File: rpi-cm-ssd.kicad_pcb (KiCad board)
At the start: 4 copper layers, 87.3 x 55.1 mm, 121 parts, among them J1 USB_C_Receptacle, J2 Bus_M.2_Socket_M, J3 PD controller EEPROM programm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, J4 ARJM11B1-502-AB-EW2, J5 690-008-221-904, U1 TVS2200DRV, U10 TPS65283-1RGER, U11 TCN75AVUA, U12 TCN75AVUA, U13 MGM210PB32JIA2, U2 TPD4EUSB30, U3 TPD4EUSB30, U4 74LVC1G07SE-7, U5 CAT24C256, U6 TPS25750DRJKT, U7 PAC1951-1, U8 USB2512, U9 SC18IS604PWJ, Y1 24MHz

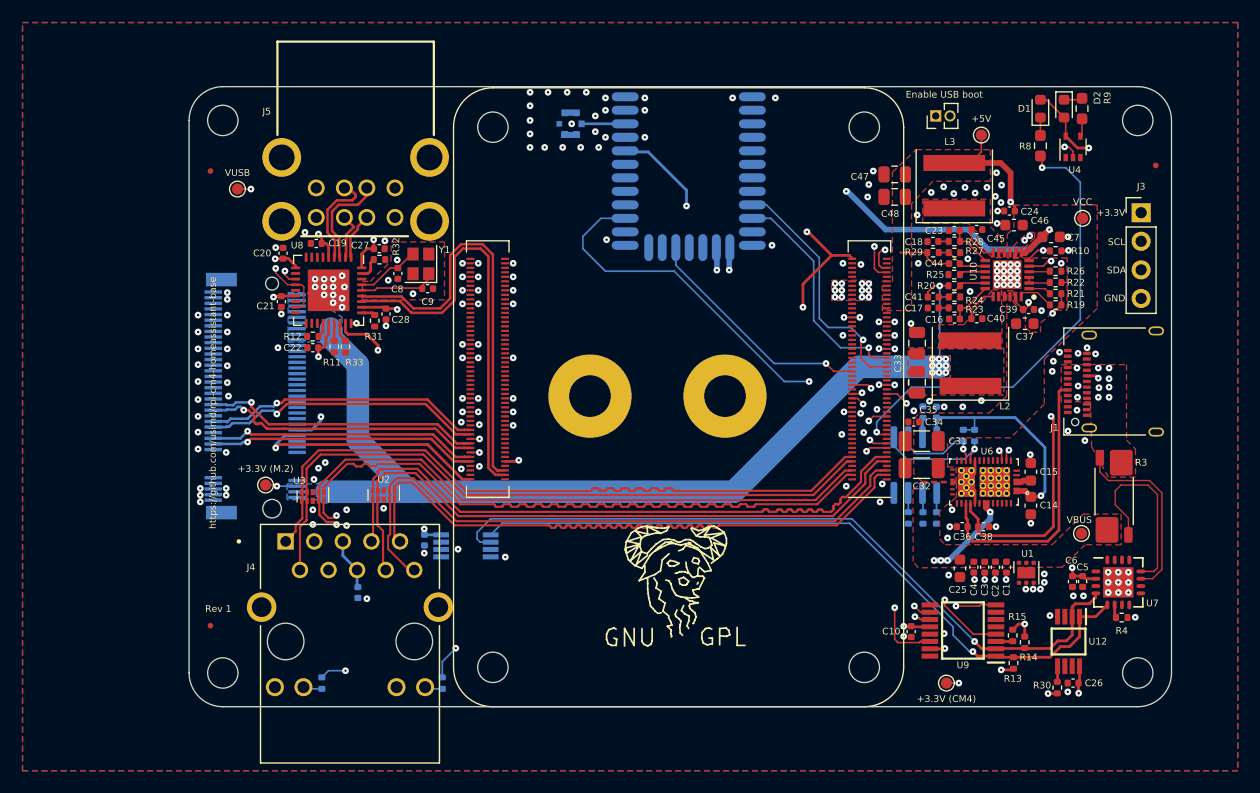
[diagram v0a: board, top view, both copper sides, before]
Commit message: Add bus debug test points
For easier debugging the I2C and SPI bus are being branched to via test
pads. Some enhancements to the PD controller are made by connecting PP5V
to ground. Also corrects the footprint of the energy meter.
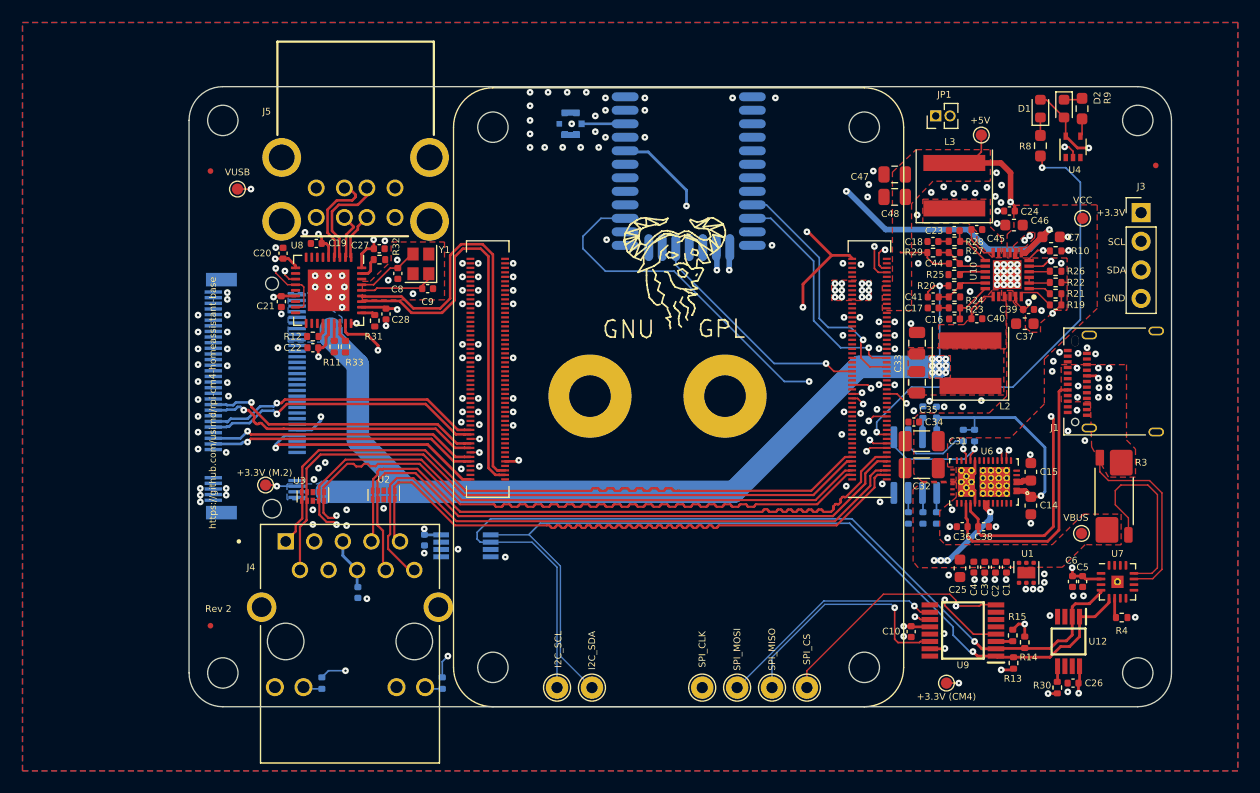
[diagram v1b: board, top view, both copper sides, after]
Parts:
- added TP10: TestPoint, TestPoint:TestPoint_THTPad_D2.0mm_Drill1.0mm, F.Cu at (73.6, 84.0)
- added TP11: TestPoint, TestPoint:TestPoint_THTPad_D2.0mm_Drill1.0mm, F.Cu at (86.5, 84.0)
- added TP12: TestPoint, TestPoint:TestPoint_THTPad_D2.0mm_Drill1.0mm, F.Cu at (95.8, 84.0)
- added TP7: TestPoint, TestPoint:TestPoint_THTPad_D2.0mm_Drill1.0mm, F.Cu at (92.7, 84.0)
- added TP8: TestPoint, TestPoint:TestPoint_THTPad_D2.0mm_Drill1.0mm, F.Cu at (76.7, 84.0)
- added TP9: TestPoint, TestPoint:TestPoint_THTPad_D2.0mm_Drill1.0mm, F.Cu at (89.6, 84.0)
- JP1: renamed from Enable USB boot
- TP1: renamed from +3.3V (CM4)
- TP4: renamed from +3.3V (M.2)
- U7: footprint Package_DFN_QFN:UQFN-16-1EP_4x4mm_P0.65mm_EP2.7x2.7mm -> Package_DFN_QFN:VQFN-16-1EP_3x3mm_P0.5mm_EP1.1x1.1mm_ThermalVias
- moved REF** 27.4 mm to (84.3, 46.0)
- moved U7 0.09 mm to (123.4, 74.6)
- renumbered 2242 to H5, 2230 to H6, VBUS to TP2, VCC to TP3, +5V to TP5, VUSB to TP6
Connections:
- U6 pad 34: unconnected-(U6-Pad34) -> GND
- U6 pad 35: unconnected-(U6-Pad35) -> GND
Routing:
- net /CM4 GPIO/SPI0_SCLK: track 24.4 -> 44.3 mm
- net /CM4 GPIO/SPI0_MOSI: track 24.4 -> 43.5 mm
- net /CM4 GPIO/SPI0_CE0: track 26.9 -> 45.2 mm
- net /Power/I2C_SCL: track 85.8 -> 103.8 mm
- net /Power/I2C_SDA: track 85.0 -> 101.5 mm
- net /CM4 GPIO/SPI0_MISO: track 27.7 -> 43.3 mm
- net Net-(R3-Pad3): track 16.9 -> 17.5 mm
- net Net-(R3-Pad2): track 16.6 -> 17.2 mm
- net Net-(R4-Pad2): track 1.17 -> 1.76 mm
- net GND: vias 218 -> 205
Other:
- board text added: "+3.3V (CM4)"
- board text added: "+3.3V (M.2)"
- board text added: "+5V"
- board text added: "2230"
- board text added: "2242"
- board text added: "I2C_SCL"
- board text added: "I2C_SDA"
- board text added: "Rev 2"
- board text added: "SPI_CLK"
- board text added: "SPI_CS"
- board text added: "SPI_MISO"
- board text added: "SPI_MOSI"
- board text added: "VBUS"
- board text added: "VCC"
- board text added: "VUSB"
- board text removed: "Rev 1"
